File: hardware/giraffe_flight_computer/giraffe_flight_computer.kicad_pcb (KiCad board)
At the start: 4 copper layers, 170 parts, among them J1 BAT+, J10 HAT ADC CONNECT, J11 SHOE ADC, J12 BAT-, J2 BAT-, J3 PCM Interface, J4 EEPROM PROG, J5 PI_HEADER_HAT, J6 BAT+, J7 PI_HEADER_SHOE, J8 Extra Audio, J9 USB, Q1 DMG2305UX, Q2 DMMT5401, Q3 NPN, Q4 NPN, Q5 NPN, U1 DS18B20, U11 TPS61033, U12 ISO6720B, U13 PCM2902C, U14 INA180A1, U15 ISO6720B, U2 CAT24C32, U3 BMI088, U4 BME280, U5 TPS61033, U6 MAX11615, U7 INA180A1, U8 SAM-M8Q, U9 AD1582B, Y1 12MHz

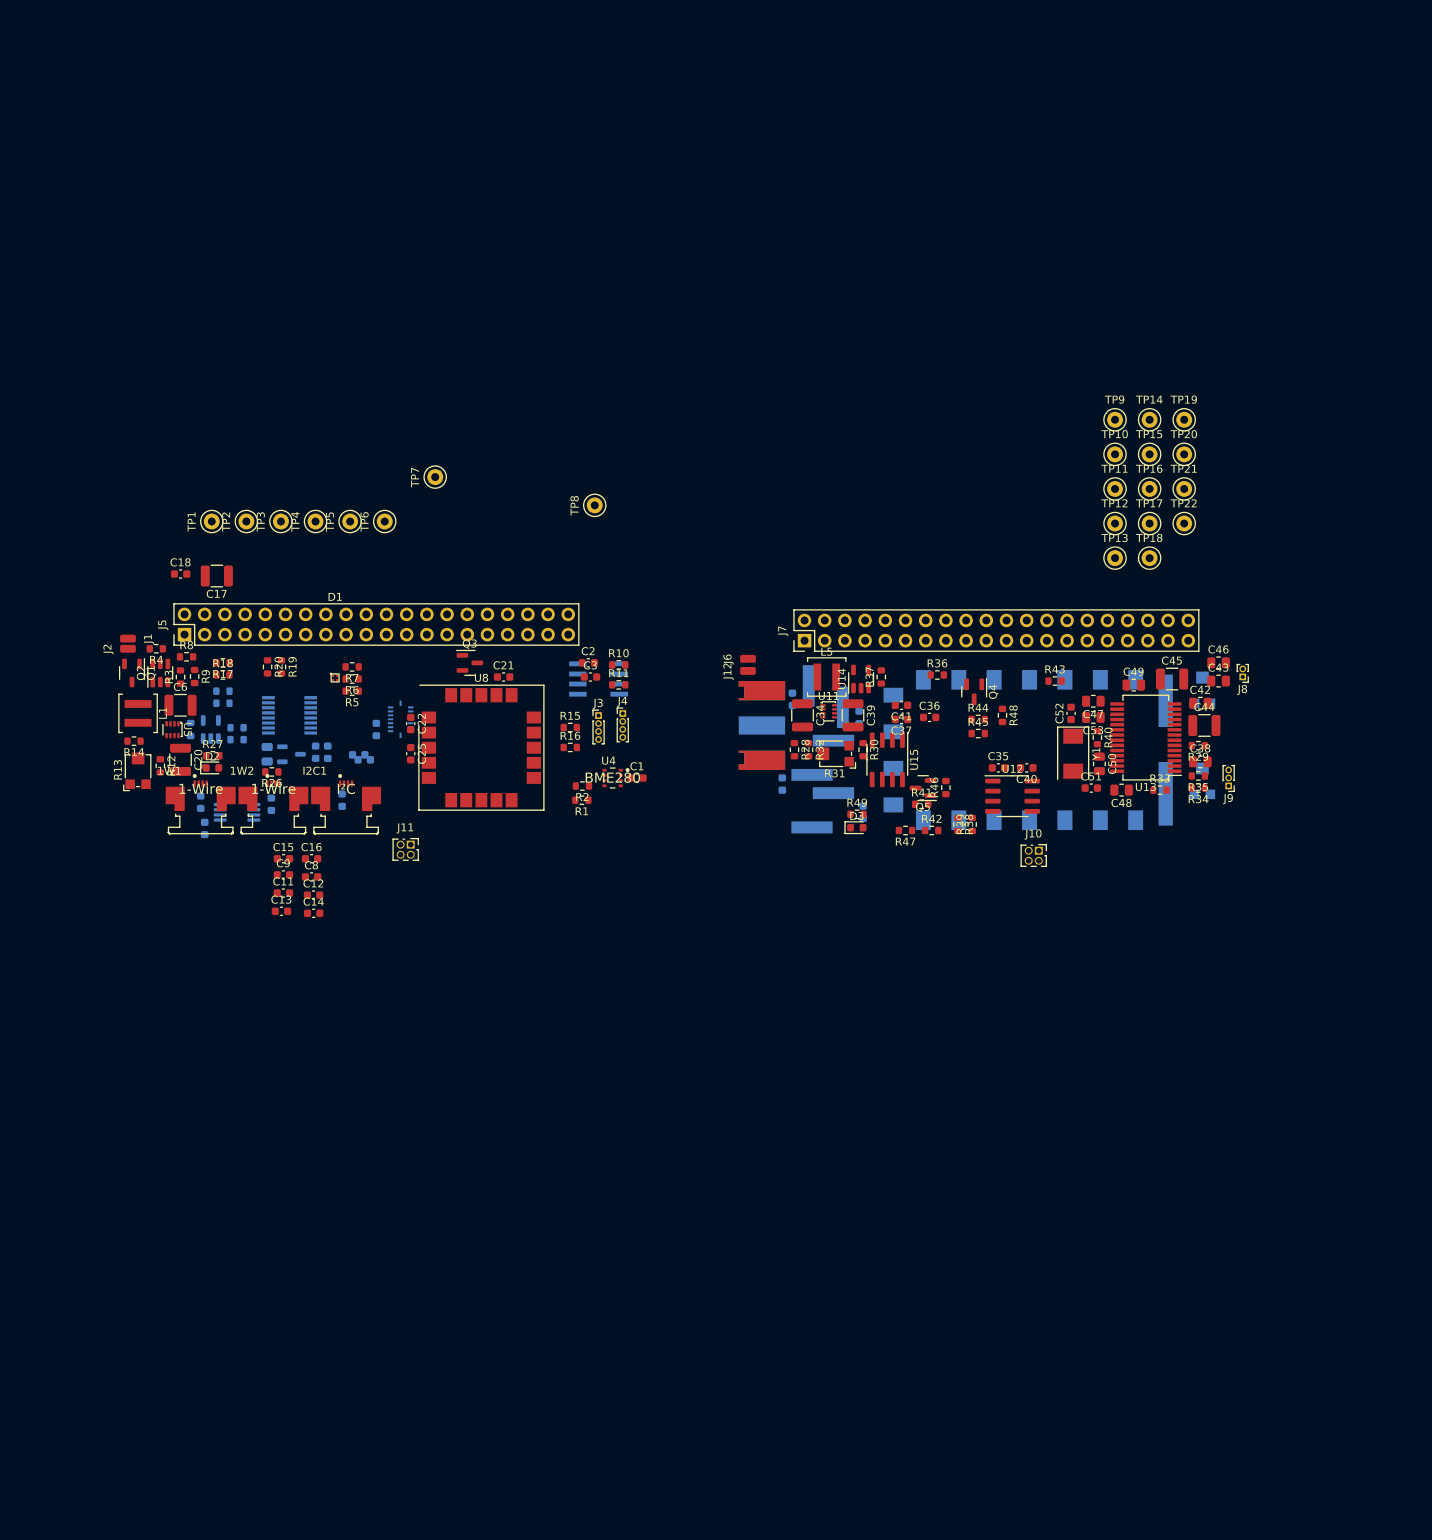
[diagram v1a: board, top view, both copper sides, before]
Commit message: More Schematic changes
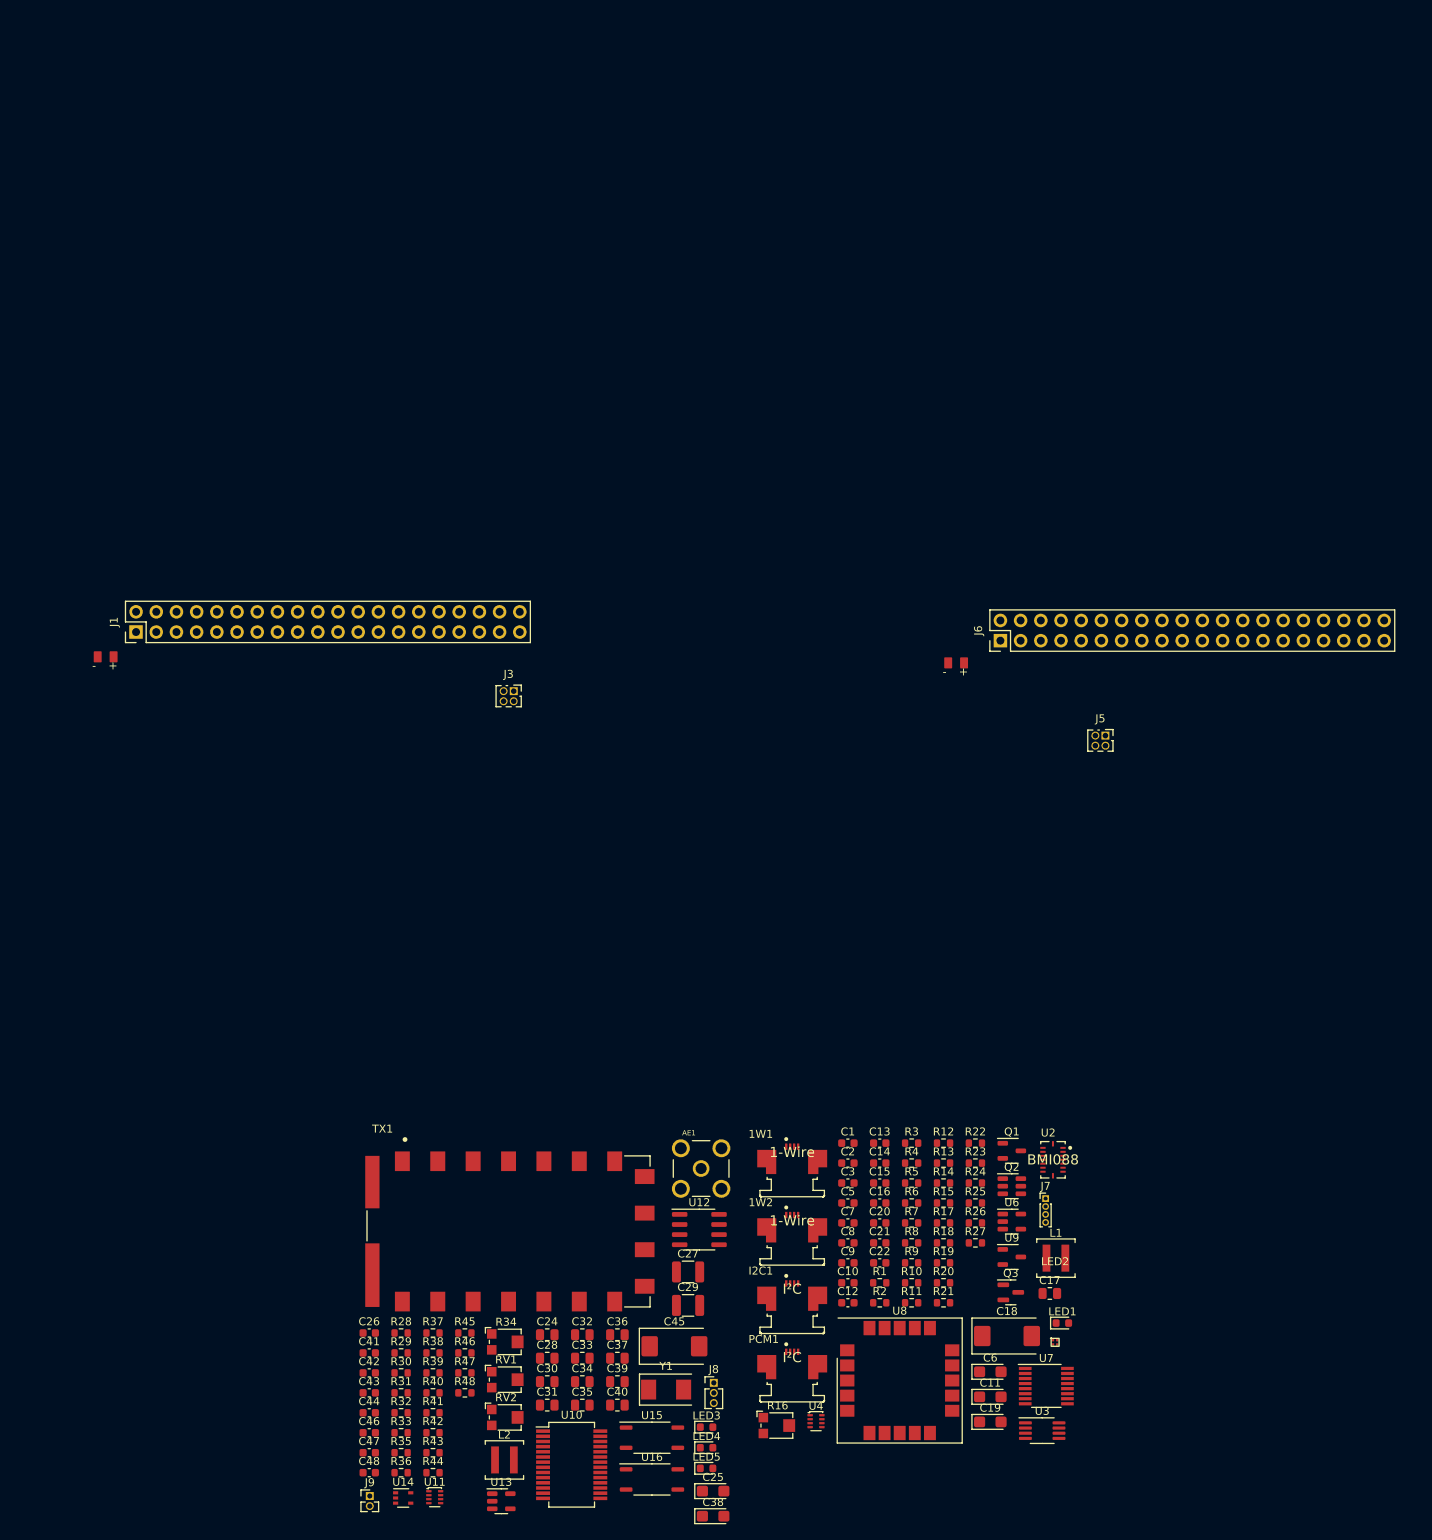
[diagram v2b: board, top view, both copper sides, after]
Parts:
- removed C23, C4: 0.1µF, Capacitor_SMD:C_0603_1608Metric
- removed C49, C50, C53: 1μF, Resistor_SMD:R_0805_2012Metric
- removed C51, C52: ?pF, Capacitor_SMD:C_0603_1608Metric
- removed D1: STATUS, giraffe_flight_computer_footprints:B36S3RGB LED
- removed D2: HAT PWR LED, LED_SMD:LED_0603_1608Metric
- removed D3: SHOE PWR LED, LED_SMD:LED_0603_1608Metric
- removed J10: HAT ADC CONNECT, Connector_PinSocket_1.27mm:PinSocket_2x02_P1.27mm_Vertical
- removed J11: SHOE ADC, Connector_PinSocket_1.27mm:PinSocket_2x02_P1.27mm_Vertical
- removed J12: BAT-, Connector_Wire:SolderWirePad_1x01_SMD_1x2mm
- removed L3: 68nH, giraffe_flight_computer_footprints:IND_AIAC-1812-33NK-T
- removed L4: 56nH, giraffe_flight_computer_footprints:IND_AIAC-1812-33NK-T
- removed L5: 0.47uH, Inductor_SMD:L_Coilcraft_XAL4020-XXX
- removed Q4, Q5: NPN, Package_TO_SOT_SMD:SOT-23
- removed R49: ?Ω, Resistor_SMD:R_0603_1608Metric
- removed TP1, TP10, TP11, TP12, TP13, TP14, TP15, TP16, TP17, TP18, TP19, TP2, TP20, TP21, TP22, TP3, TP4, TP5, TP6, TP7, TP8, TP9: ~, TestPoint:TestPoint_Keystone_5000-5004_Miniature
- removed U1: DS18B20, Package_SO:MSOP-8_3x3mm_P0.65mm
- removed U5: TPS61033, Package_TO_SOT_SMD:SOT-583-8
- added C10: 0.1µF, Capacitor_SMD:C_0603_1608Metric, F.Cu at (124.3, 104.9)
- added LED1: PWR, LED_SMD:LED_0603_1608Metric, F.Cu at (151.3, 110.0)
- added LED2: STATUS, giraffe_flight_computer_footprints:B36S3RGB LED, F.Cu at (150.4, 112.4)
- added LED3: PWR, LED_SMD:LED_0603_1608Metric, F.Cu at (106.6, 123.0)
- added LED4: RX, LED_SMD:LED_0603_1608Metric, F.Cu at (106.6, 125.6)
- added LED5: PTT, LED_SMD:LED_0603_1608Metric, F.Cu at (106.6, 128.2)
- added PCM1: I²C, giraffe_flight_computer_footprints:Molex-52745-0497, F.Cu at (117.3, 114.3)
- added U10: PCM2902C, Package_SO:SSOP-28_5.3x10.2mm_P0.65mm, F.Cu at (89.6, 127.8)
- added U16: TLP185, Package_SO:SOIC-4_4.55x3.7mm_P2.54mm, F.Cu at (99.7, 129.6)
- AE1: value SMA -> ~; footprint giraffe_flight_computer_footprints:MolexSmaConnector -> giraffe_flight_computer_footprints:LINX_CONSMA001-G; moved to F.Cu
- C11: value 100pF -> 10μF; footprint Capacitor_SMD:C_0603_1608Metric -> Capacitor_Tantalum_SMD:CP_EIA-3216-18_Kemet-A
- C12, C13, C14, C15, C16, C8, C9: value 100pF -> 0.1µF
- C17, C34: value 10μF -> 1μF; footprint Resistor_SMD:R_1210_3225Metric -> Resistor_SMD:R_0805_2012Metric
- C18: value 0.1µF -> 100μF; footprint Capacitor_SMD:C_0603_1608Metric -> Capacitor_Tantalum_SMD:CP_EIA-7343-31_Kemet-D
- C19: value 0.1µF -> 10μF; footprint Capacitor_SMD:C_0603_1608Metric -> Capacitor_Tantalum_SMD:CP_EIA-3216-18_Kemet-A; moved to F.Cu
- C20: value 10μF -> 0.1µF; footprint Resistor_SMD:R_1210_3225Metric -> Capacitor_SMD:C_0603_1608Metric
- C24, C5, C7, TX1, U9: moved to F.Cu
- C25: value 0.1µF -> 10μF; footprint Capacitor_SMD:C_0603_1608Metric -> Capacitor_Tantalum_SMD:CP_EIA-3216-18_Kemet-A
- C26: value 0.1µF -> 1μF; moved to F.Cu
- C27, C29: value 0.1µF -> 10μF; footprint Capacitor_SMD:C_0603_1608Metric -> Resistor_SMD:R_1210_3225Metric; moved to F.Cu
- C28: value 0.1µF -> 0.1μF; footprint Capacitor_SMD:C_0603_1608Metric -> Resistor_SMD:R_0805_2012Metric; moved to F.Cu
- C30: value 20pF -> 1uF; footprint Capacitor_SMD:C_0603_1608Metric -> Resistor_SMD:R_0805_2012Metric; moved to F.Cu
- C31: value 36pF -> 1μF; footprint Capacitor_SMD:C_0603_1608Metric -> Resistor_SMD:R_0805_2012Metric; moved to F.Cu
- C32: value 36pF -> 0.1μF; footprint Capacitor_SMD:C_0603_1608Metric -> Resistor_SMD:R_0805_2012Metric; moved to F.Cu
- C33: value 20pF -> 1μF; footprint Capacitor_SMD:C_0603_1608Metric -> Resistor_SMD:R_0805_2012Metric; moved to F.Cu
- C35, C36: value 0.1µF -> 1μF; footprint Capacitor_SMD:C_0603_1608Metric -> Resistor_SMD:R_0805_2012Metric
- C37: value 10kpF -> 1μF; footprint Capacitor_SMD:C_0603_1608Metric -> Resistor_SMD:R_0805_2012Metric
- C38: value 1μF -> 10μF; footprint Resistor_SMD:R_0805_2012Metric -> Capacitor_Tantalum_SMD:CP_EIA-3216-18_Kemet-A
- C39: value 10μF -> 0.1μF; footprint Resistor_SMD:R_1210_3225Metric -> Resistor_SMD:R_0805_2012Metric
- C40: value 0.1µF -> 0.1μF; footprint Capacitor_SMD:C_0603_1608Metric -> Resistor_SMD:R_0805_2012Metric
- C41: value 1kpF -> 0.1µF
- C42: value 1μF -> 10kpF; footprint Resistor_SMD:R_0805_2012Metric -> Capacitor_SMD:C_0603_1608Metric
- C43: value 1μF -> 1kpF; footprint Resistor_SMD:R_0805_2012Metric -> Capacitor_SMD:C_0603_1608Metric
- C44: value 10μF -> 20pF; footprint Resistor_SMD:R_1210_3225Metric -> Capacitor_SMD:C_0603_1608Metric
- C45: value 10μF -> 100μF; footprint Resistor_SMD:R_1210_3225Metric -> Capacitor_Tantalum_SMD:CP_EIA-7343-31_Kemet-D
- C46, C47: value 1μF -> 36pF; footprint Resistor_SMD:R_0805_2012Metric -> Capacitor_SMD:C_0603_1608Metric
- C48: value 1μF -> 20pF; footprint Resistor_SMD:R_0805_2012Metric -> Capacitor_SMD:C_0603_1608Metric
- C6: footprint Resistor_SMD:R_1210_3225Metric -> Capacitor_Tantalum_SMD:CP_EIA-3216-18_Kemet-A
- J1, J6: value BAT+ -> PI; footprint Connector_Wire:SolderWirePad_1x01_SMD_1x2mm -> giraffe_flight_computer_footprints:pi_zero
- J2: value BAT- -> BAT; footprint Connector_Wire:SolderWirePad_1x01_SMD_1x2mm -> giraffe_flight_computer_footprints:battery_connection
- J3: value PCM Interface -> ADC; footprint Connector_PinHeader_1.00mm:PinHeader_1x04_P1.00mm_Vertical -> Connector_PinSocket_1.27mm:PinSocket_2x02_P1.27mm_Vertical
- J4: value EEPROM PROG -> BAT; footprint Connector_PinHeader_1.00mm:PinHeader_1x04_P1.00mm_Vertical -> giraffe_flight_computer_footprints:battery_connection
- J5: value PI_HEADER_HAT -> ADC; footprint giraffe_flight_computer_footprints:pi_zero -> Connector_PinSocket_1.27mm:PinSocket_2x02_P1.27mm_Vertical
- J7: value PI_HEADER_SHOE -> ~; footprint giraffe_flight_computer_footprints:pi_zero -> Connector_PinHeader_1.00mm:PinHeader_1x04_P1.00mm_Vertical
- J8: value Extra Audio -> USB; footprint Connector_PinHeader_1.00mm:PinHeader_1x02_P1.00mm_Vertical -> Connector_PinHeader_1.27mm:PinHeader_1x03_P1.27mm_Vertical
- J9: value USB -> EXT_AUDIO; footprint Connector_PinHeader_1.00mm:PinHeader_1x03_P1.00mm_Vertical -> Connector_PinHeader_1.27mm:PinHeader_1x02_P1.27mm_Vertical
- L2: value 56nH -> 0.47uH; footprint giraffe_flight_computer_footprints:IND_AIAC-1812-33NK-T -> Inductor_SMD:L_Coilcraft_XAL4020-XXX; moved to F.Cu
- R1: value 0Ω -> ?Ω
- R10: value 3.9kΩ -> ?
- R11: value 3.9kΩ -> 4.7kΩ
- R12: value 21.5KΩ -> ?
- R13: value 1kΩ -> ?; footprint Potentiometer_SMD:Potentiometer_Bourns_TC33X_Vertical -> Resistor_SMD:R_0603_1608Metric
- R14: value 3kΩ -> 0Ω
- R15: value ?Ω -> 21.5k
- R16: value ?Ω -> 1k; footprint Resistor_SMD:R_0603_1608Metric -> Potentiometer_SMD:Potentiometer_Bourns_TC33X_Vertical
- R17: value ?Ω -> 3k
- R18, R48: value ?Ω -> 0Ω
- R19: value * -> ?Ω
- R2: value 0Ω -> ?
- R20: value * -> ?
- R21, R22, R23: value ?Ω -> ?; moved to F.Cu
- R24, R25: value ?Ω -> *; moved to F.Cu
- R26: value 4.7kΩ -> ?Ω
- R28: value ?Ω -> 22Ω
- R29: value 2.2Ω -> 22Ω
- R3, R37, R38, R41, R9: value ?Ω -> ?
- R30: value ?Ω -> 1.5kΩ
- R31: footprint Potentiometer_SMD:Potentiometer_Bourns_TC33X_Vertical -> Resistor_SMD:R_0603_1608Metric
- R32: value ?Ω -> 1MΩ
- R33: value 1.5kΩ -> ?k
- R34: value 22Ω -> ?k; footprint Resistor_SMD:R_0603_1608Metric -> Potentiometer_SMD:Potentiometer_Bourns_TC33X_Vertical
- R35: value 22Ω -> ?k
- R36: value 10kΩ -> ?Ω
- R39: value ?Ω -> 10kΩ
- R4, R5: value ?Ω -> 3.9kΩ
- R40: value 1MΩ -> ?
- R42: value ?Ω -> ?k
- R44, R47: value ?kΩ -> ?Ω
- RV1, RV2: value 100kΩ -> 100k; moved to F.Cu
- U13: value PCM2902C -> INA180A1; footprint Package_SO:SSOP-28_5.3x10.2mm_P0.65mm -> Package_TO_SOT_SMD:SOT-23-5
- U14: value INA180A1 -> 74LVC1G04; footprint Package_TO_SOT_SMD:SOT-23-5 -> Package_TO_SOT_SMD:SOT-353_SC-70-5
- U15: value ISO6720B -> TLP185; footprint Package_SO:SOIC-8_3.9x4.9mm_P1.27mm -> Package_SO:SOIC-4_4.55x3.7mm_P2.54mm
- U2: value CAT24C32 -> BMI088; footprint giraffe_flight_computer_footprints:CAT24C32WI_GT3 -> giraffe_flight_computer_footprints:BMI088; moved to F.Cu
- U3: value BMI088 -> DS18B20; footprint giraffe_flight_computer_footprints:BMI088 -> Package_SO:MSOP-8_3x3mm_P0.65mm; moved to F.Cu
- U4: value BME280 -> TPS61033; footprint giraffe_flight_computer_footprints:BME280 -> Package_TO_SOT_SMD:SOT-583-8
- U6: value MAX11615 -> INA180A1; footprint Package_SO:QSOP-16_3.9x4.9mm_P0.635mm -> Package_TO_SOT_SMD:SOT-23-5; moved to F.Cu
- U7: value INA180A1 -> MAX11615; footprint Package_TO_SOT_SMD:SOT-23-5 -> Package_SO:QSOP-16_3.9x4.9mm_P0.635mm; moved to F.Cu
- moved C46 144.2 mm to (64.1, 123.8)
- moved C18 141.4 mm to (144.3, 111.6)
- moved J9 140.2 mm to (64.2, 131.7), turned to 0 degrees
- moved C43 139.4 mm to (64.1, 118.7)
- moved C17 138.3 mm to (149.7, 106.2), turned to 0 degrees
- moved C44 136.0 mm to (64.1, 121.2)
- moved C42 134.2 mm to (64.1, 116.2)
- moved L1 134.2 mm to (150.5, 101.8), turned to 0 degrees
- moved U7 133.7 mm to (149.3, 117.9), turned to 0 degrees
- moved C6 131.9 mm to (142.2, 116.1)
- moved R35 131.5 mm to (68.1, 126.3), turned to 0 degrees
- moved C47 131.3 mm to (64.1, 126.3), turned to 0 degrees
- moved C48 127.8 mm to (64.1, 128.8), turned to 0 degrees
- moved R29 126.0 mm to (68.1, 113.7), turned to 0 degrees
- moved Q1 125.9 mm to (144.9, 88.3), turned to 0 degrees
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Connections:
- 1W1 pad 2: 1-Wire -> /hat/1_WIRE
- 1W1 pad 3: H_3V3 -> Net-(1W1-Pin_3)
- 1W2 pad 2: 1-Wire -> /hat/1_WIRE
- 1W2 pad 3: H_3V3 -> Net-(1W2-Pin_3)
- AE1 pad 1: /RF_OUT_FILTERED -> /shoe/RF_OUT_FILTERED
- C1 pad 1: H_GND -> H_3V3
- C1 pad 2: H_3V3 -> H_GND
- C11 pad 1: H_GND -> Net-(U4-VOUT)
- C11 pad 2: ADC CH2 -> H_GND
- C12 pad 1: H_GND -> H_3V3
- C12 pad 2: Net-(J11-Pin_2) -> Net-(1W2-Pin_3)
- C13 pad 1: H_GND -> H_3V3
- C13 pad 2: ADC CH1 -> H_GND
- C14 pad 1: H_GND -> H_3V3
- C14 pad 2: Net-(J11-Pin_3) -> H_GND
- C15 pad 1: H_GND -> H_3V3
- C15 pad 2: ADC CH0 -> H_GND
- C16 pad 1: H_GND -> H_3V3
- C16 pad 2: Net-(J11-Pin_4) -> H_GND
- C17 pad 1: H_5V_HAT -> Net-(U7-REF)
- C18 pad 1: H_GND -> H_5V_HAT
- C18 pad 2: H_5V_HAT -> H_GND
- C19 pad 1: H_3V3 -> H_5V_HAT
- C20 pad 1: Net-(U5-VOUT) -> H_GND
- C20 pad 2: H_GND -> H_5V_HAT
- C21 pad 1: H_3V3 -> H_5V_HAT
- C22 pad 1: H_3V3 -> H_5V_HAT
- C24 pad 1: Net-(U6-REF) -> S_5V
- C24 pad 2: H_GND -> S_GND
- C25 pad 1: H_3V3 -> /shoe/+BATT
- C25 pad 2: H_GND -> S_GND
- C26 pad 1: H_GND -> S_GND
- C26 pad 2: H_3V3 -> Net-(U10-SEL0)
- C27 pad 1: H_GND -> Net-(U10-VCCCI)
- C27 pad 2: H_3V3 -> S_GND
- C28 pad 1: H_5V_HAT -> S_GND
- C28 pad 2: H_GND -> S_3V3
- C29 pad 1: H_5V_HAT -> Net-(U10-VCOM)
- C29 pad 2: H_GND -> S_GND
- C30 pad 1: SA868_RF_OUT -> S_GND
- C30 pad 2: S_GND -> Net-(U10-VCCP1I)
- C31 pad 1: Net-(C31-Pad1) -> S_GND
- C31 pad 2: S_GND -> Net-(U10-VCCP2I)
- C32 pad 1: Net-(C32-Pad1) -> S_4V
- C33 pad 1: /RF_OUT_FILTERED -> S_GND
- C33 pad 2: S_GND -> Net-(U10-VCCXI)
- C34 pad 1: Net-(J6-Pin_1) -> Net-(U10-VOUTR)
- C34 pad 2: S_GND -> /shoe/AUDIO_IN_RIGHT
- C35 pad 1: S_3V3 -> Net-(U10-VINR)
- C35 pad 2: S_GND -> /shoe/AUDIO_OUT_RIGHT
- C36 pad 1: S_GND -> Net-(U10-VOUTL)
- C36 pad 2: S_4V -> /shoe/AUDIO_OUT_LEFT
- C37 pad 1: S_GND -> Net-(U10-VINL)
- C37 pad 2: S_4V -> /shoe/AUDIO_IN_LEFT
- C38 pad 1: /VBUS -> Net-(U11-VOUT)
- C39 pad 1: Net-(U11-VOUT) -> Net-(U10-XTI)
- C40 pad 1: S_4V -> Net-(U10-XTO)
- C42 pad 1: Net-(U13-VINL) -> S_GND
- C42 pad 2: PCM_AUDIO.IN_L -> S_4V
- C43 pad 1: Net-(U13-VINR) -> S_GND
- C43 pad 2: PCM_AUDIO.IN_R -> S_4V
- C44 pad 1: Net-(U13-VCCCI) -> Net-(TX1-ANT)
- C45 pad 1: Net-(U13-VCOM) -> S_4V
- C46 pad 1: Net-(U13-VOUTR) -> Net-(C46-Pad1)
- C46 pad 2: PCM_AUDIO.OUT_R -> S_GND
- C47 pad 1: Net-(U13-VCCP1I) -> Net-(C47-Pad1)
- C48 pad 1: Net-(U13-SEL0) -> /shoe/RF_OUT_FILTERED
- C6 pad 1: /Battery Polarized -> Net-(Q1-S)
- C8 pad 2: ADC CH3 -> H_3V3
- C9 pad 2: Net-(J11-Pin_1) -> H_3V3
- I2C1 pad 3: I2C0.SCL -> /hat/I2C0.SCL
- I2C1 pad 4: I2C0.SDA -> /hat/I2C0.SDA
- J1 pad 1: Net-(J1-Pin_1) -> /hat/3V3
- J2 pad 1: H_GND -> /hat/-BATT
- J3 pad 1: /PCM.DOUT -> /hat/ADC.CH4
- J3 pad 2: /PCM.DIN -> /hat/ADC.CH5
- J3 pad 3: /PCM.FS -> /hat/ADC.CH6
- J3 pad 4: /PCM.CLK -> /hat/ADC.CH7
- J4 pad 1: H_GND -> /shoe/-BATT
- J4 pad 2: H_3V3 -> /shoe/+BATT
- J5 pad 1: H_3V3 -> /shoe/ADC_CH4
- J5 pad 2: H_5V_HAT -> /shoe/ADC_CH5
- J5 pad 3: I2C0.SDA -> unconnected-(J5-Pin_3-Pad3)
- J5 pad 4: H_5V_HAT -> unconnected-(J5-Pin_4-Pad4)
- J6 pad 1: Net-(J6-Pin_1) -> /shoe/3V3
- J7 pad 1: S_3V3 -> H_GND
- J7 pad 2: S_5V -> H_3V3
- J7 pad 3: unconnected-(J7-SDA/GPIO2-Pad3) -> /hat/EEPROM.SCL
- J7 pad 4: S_5V -> /hat/EEPROM.SDA
- J8 pad 1: PCM_AUDIO.IN_R -> S_GND
- J8 pad 2: PCM_AUDIO.OUT_R -> Net-(J8-Pin_2)
- J9 pad 1: Net-(J9-Pin_1) -> S_GND
- J9 pad 2: Net-(J9-Pin_2) -> /shoe/AUDIO_OUT_RIGHT
- L1 pad 1: /Battery Polarized -> Net-(Q1-S)
- L1 pad 2: Net-(U5-SW) -> Net-(U4-SW)
- L2 pad 1: SA868_RF_OUT -> /shoe/+BATT
- L2 pad 2: Net-(C31-Pad1) -> Net-(U11-SW)
- Q1 pad 1: Net-(J1-Pin_1) -> /hat/+BATT
- Q1 pad 3: /Battery Polarized -> Net-(Q1-S)
- Q2 pad 5: /Battery Polarized -> Net-(Q1-S)
- Q2 pad 6: Net-(J1-Pin_1) -> /hat/+BATT
- R1 pad 1: H_3V3 -> H_5V_HAT
- R1 pad 2: Net-(U4-SDO) -> Net-(LED1-A)
- R10 pad 1: EEPROM.SDA -> Net-(U7-AIN0)
- R10 pad 2: H_3V3 -> H_GND
- R11 pad 1: EEPROM.SCL -> H_3V3
- R11 pad 2: H_3V3 -> /hat/1_WIRE
- R12 pad 1: Net-(U5-VOUT) -> /hat/3V3
- R12 pad 2: Net-(R12-Pad2) -> Net-(U7-AIN3)
- R13 pad 1: Net-(R12-Pad2) -> Net-(U7-AIN3)
- R13 pad 2: Net-(U5-FB) -> H_GND
- R14 pad 1: Net-(U5-FB) -> Net-(U5-SDO)
- R15 pad 1: Net-(Q3-C) -> Net-(U4-VOUT)
- R15 pad 2: H_3V3 -> Net-(R15-Pad2)
- R16 pad 1: Net-(Q3-B) -> Net-(R15-Pad2)
- R16 pad 2: SAM-M8Q.RST -> Net-(U4-FB)
- R17 pad 1: H_3V3 -> Net-(U4-FB)
- R17 pad 2: ADC CH3 -> H_GND
- R18 pad 1: ADC CH3 -> Net-(U5-SDO)
- R18 pad 2: H_GND -> H_3V3
- R19 pad 1: I2C0.SDA -> Net-(U4-VOUT)
- R19 pad 2: H_3V3 -> H_5V_HAT
- R2 pad 1: Net-(U4-SDO) -> Net-(Q2-B1)
- R20 pad 1: H_3V3 -> Net-(U6-OUT)
- R20 pad 2: I2C0.SCL -> Net-(U7-AIN1)
- R21 pad 1: Net-(U5-VOUT) -> Net-(U7-AIN1)
- R21 pad 2: H_5V_HAT -> H_GND
- R22 pad 1: Net-(U7-OUT) -> H_5V_HAT
- R22 pad 2: ADC CH1 -> Net-(U7-AIN2)
- R23 pad 1: ADC CH1 -> Net-(U7-AIN2)
- R24 pad 1: H_5V_HAT -> /hat/I2C0.SDA
- R24 pad 2: ADC CH2 -> H_3V3
- R25 pad 1: ADC CH2 -> H_3V3
- R25 pad 2: H_GND -> /hat/I2C0.SCL
- R26 pad 1: H_3V3 -> Net-(Q3-C)
- R26 pad 2: 1-Wire -> H_3V3
- R27 pad 1: H_5V_HAT -> Net-(Q3-B)
- R27 pad 2: Net-(D2-A) -> /hat/SAM_M8Q.RST
- R28 pad 1: SA868.PWR -> Net-(J8-Pin_3)
- R28 pad 2: S_GND -> Net-(U10-D+)
- R29 pad 1: S_5V -> Net-(J8-Pin_2)
- R29 pad 2: /VBUS -> Net-(U10-D-)
- R3 pad 1: Net-(Q2-B1) -> Net-(Q1-G)
- R30 pad 1: Net-(U11-VOUT) -> Net-(U10-SEL0)
- R30 pad 2: Net-(R30-Pad2) -> Net-(U10-D+)
- R31 pad 1: Net-(R30-Pad2) -> /shoe/SA868_PWR_CTRL
- R31 pad 2: Net-(U11-FB) -> S_GND
- R32 pad 1: Net-(U11-FB) -> Net-(U10-XTO)
- R32 pad 2: S_GND -> Net-(U10-XTI)
- R33 pad 1: Net-(U13-SEL0) -> Net-(U11-VOUT)
- R33 pad 2: Net-(J9-Pin_1) -> Net-(R33-Pad2)
- R34 pad 1: Net-(J9-Pin_1) -> Net-(R33-Pad2)
- R34 pad 2: Net-(U13-D+) -> Net-(U11-FB)
- R35 pad 1: Net-(J9-Pin_2) -> Net-(U11-FB)
- R35 pad 2: Net-(U13-D-) -> S_GND
- R36 pad 1: S_4V -> Net-(U11-VOUT)
- R36 pad 2: Net-(TX1-PD) -> S_4V
- R37 pad 1: Net-(U11-VOUT) -> Net-(U13-OUT)
- R37 pad 2: S_4V -> /shoe/ADC_CH4
- R38 pad 1: Net-(U14-OUT) -> /shoe/ADC_CH4
- R38 pad 2: ADC CH4 -> S_GND
- R39 pad 1: ADC CH4 -> Net-(TX1-PD)
- R39 pad 2: S_GND -> S_4V
- R4 pad 1: Net-(Q1-G) -> /hat/EEPROM.SDA
- R4 pad 2: H_GND -> H_3V3
- R40 pad 1: Net-(U13-XTO) -> S_4V
- R40 pad 2: Net-(U13-XTI) -> /shoe/ADC_CH5
- R41 pad 1: S_4V -> /shoe/ADC_CH5
- R41 pad 2: ADC CH5 -> S_GND
- R42 pad 1: ADC CH5 -> Net-(TX1-PTT)
- R42 pad 2: S_GND -> Net-(R42-Pad2)
- R43 pad 1: Net-(Q5-B) -> Net-(R43-Pad1)
- R44 pad 1: S_GND -> S_4V
- R44 pad 2: Net-(Q4-B) -> Net-(LED3-A)
- R45 pad 1: Net-(Q4-C) -> /shoe/SA868_RX
- R45 pad 2: S_4V -> Net-(LED4-A)
- R46 pad 1: S_4V -> /shoe/SA868_PTT
- R46 pad 2: Net-(Q5-C) -> Net-(R46-Pad2)
- R47 pad 1: S_GND -> /shoe/SA868_PTT
- R47 pad 2: Net-(Q5-B) -> Net-(LED5-A)
- R48 pad 1: Net-(Q4-B) -> S_GND
- R48 pad 2: Net-(U15-OUTB) -> Net-(TX1-H/L)
- R5 pad 1: /Status LED Red -> /hat/EEPROM.SCL
- R5 pad 2: Net-(D1-RK) -> H_3V3
- R6 pad 1: /Status LED Green -> /hat/STATUS_LED.RED
- R7 pad 1: /Status LED Blue -> /hat/STATUS_LED.GREEN
- R8 pad 1: /Battery Polarized -> /hat/STATUS_LED.BLUE
- R8 pad 2: ADC CH0 -> Net-(LED2-BA)
- R9 pad 1: ADC CH0 -> Net-(Q1-S)
- R9 pad 2: H_GND -> Net-(U7-AIN0)
- RV1 pad 2: SA868_AUDIO_OUT -> Net-(TX1-MIC_IN)
- RV1 pad 3: PCM_AUDIO.IN_L -> /shoe/AUDIO_OUT_LEFT
- RV2 pad 2: PCM_AUDIO.OUT_L -> /shoe/AUDIO_IN_LEFT
- RV2 pad 3: SA868_AUDIO_IN -> Net-(TX1-AF_OUT)
- TX1 pad 12: SA868_RF_OUT -> Net-(TX1-ANT)
- TX1 pad 18: SA868_AUDIO_IN -> Net-(TX1-MIC_IN)
- TX1 pad 3: SA868_AUDIO_OUT -> Net-(TX1-AF_OUT)
- TX1 pad 5: Net-(Q4-C) -> Net-(TX1-PTT)
- TX1 pad 7: Net-(SW2-B) -> Net-(TX1-H/L)
- U11 pad 1: Net-(J6-Pin_1) -> /shoe/+BATT
- U11 pad 2: SA868.PWR -> /shoe/SA868_PWR_CTRL
- U12 pad 2: UART.RXD -> /shoe/UART.RX
- U12 pad 3: UART.TXD -> /shoe/UART.TX
- U13 pad 1: Net-(U13-D+) -> Net-(U13-OUT)
- U13 pad 2: Net-(U13-D-) -> S_GND
- U13 pad 3: /VBUS -> Net-(U11-VOUT)
- U13 pad 4: S_GND -> S_4V
- U13 pad 5: unconnected-(U13-HID0-Pad5) -> S_5V
- U14 pad 1: Net-(U14-OUT) -> (no net)
- U14 pad 2: S_GND -> Net-(U14-Pad2)
- U14 pad 3: Net-(U11-VOUT) -> S_GND
- U14 pad 4: S_4V -> Net-(R42-Pad2)
- U14 pad 5: S_5V -> S_4V
- U15 pad 1: S_3V3 -> Net-(R43-Pad1)
- U15 pad 3: SA868.PTT -> S_GND
- U15 pad 4: S_GND -> /shoe/SA868_RX
- U15 pad 6: Net-(U15-OUTB) -> S_3V3
- U2 pad 1: H_GND -> unconnected-(U2-INT2-Pad1)
- U2 pad 3: H_GND -> H_3V3
- U2 pad 5: EEPROM.SDA -> /hat/SPI0.CE1
- U2 pad 6: EEPROM.SCL -> H_GND
- U2 pad 7: unconnected-(U2-WP-Pad7) -> H_GND
- U2 pad 8: H_3V3 -> /hat/SPI0.SCLK
- U3 pad 2: H_GND -> unconnected-(U3-NC-Pad2)
- U3 pad 4: H_GND -> /hat/1_WIRE
- U3 pad 5: SPI0.CE1 -> H_GND
- U3 pad 6: H_GND -> unconnected-(U3-NC-Pad6)
- U3 pad 7: H_GND -> unconnected-(U3-NC-Pad7)
- U3 pad 8: SPI0.SCLK -> unconnected-(U3-NC-Pad8)
- U4 pad 1: H_GND -> Net-(Q1-S)
- U4 pad 2: H_3V3 -> Net-(Q1-S)
- U4 pad 3: I2C0.SDA -> H_GND
- U4 pad 4: I2C0.SCL -> Net-(U4-PG)
- U4 pad 5: Net-(U4-SDO) -> Net-(U4-FB)
- U4 pad 6: H_3V3 -> H_GND
- U4 pad 7: H_GND -> Net-(U4-SW)
- U4 pad 8: H_3V3 -> Net-(U4-VOUT)
- U6 pad 1: Net-(U6-REF) -> Net-(U6-OUT)
- U6 pad 2: unconnected-(U6-NC-Pad2) -> H_GND
- U6 pad 3: unconnected-(U6-NC-Pad3) -> Net-(U4-VOUT)
- U6 pad 4: unconnected-(U6-NC-Pad4) -> H_5V_HAT
- U6 pad 5: ADC CH0 -> H_5V_HAT
- U7 pad 1: Net-(U7-OUT) -> Net-(U7-REF)
- U7 pad 2: H_GND -> unconnected-(U7-NC-Pad2)
- U7 pad 3: Net-(U5-VOUT) -> unconnected-(U7-NC-Pad3)
- U7 pad 4: H_5V_HAT -> unconnected-(U7-NC-Pad4)
- U7 pad 5: H_5V_HAT -> Net-(U7-AIN0)
- U8 pad 12: I2C0.SCL -> /hat/I2C0.SCL
- U8 pad 13: SAM-M8Q.TX_RDY -> /hat/SAM_M8Q.TX_RDY
- U8 pad 9: I2C0.SDA -> /hat/I2C0.SDA
- U9 pad 1: Net-(U6-REF) -> Net-(U7-REF)
- Y1 pad 1: Net-(U13-XTO) -> Net-(U10-XTO)
- Y1 pad 2: Net-(U13-XTI) -> Net-(U10-XTI)

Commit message: Rev A Hat Complete
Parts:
- removed C12: 0.1µF, Capacitor_SMD:C_0603_1608Metric
- removed Q1: DMG2305UX, Package_TO_SOT_SMD:SOT-23-3
- removed Q2: DMMT5401, Package_TO_SOT_SMD:SOT-23-6
- removed R21, R37, R38: ?, Resistor_SMD:R_0603_1608Metric
- removed R31, R36: ?Ω, Resistor_SMD:R_0603_1608Metric
- removed R34: ?k, Potentiometer_SMD:Potentiometer_Bourns_TC33X_Vertical
- removed U13, U6: INA180A1, Package_TO_SOT_SMD:SOT-23-5
- added C4: 0.1µF, Capacitor_SMD:C_0603_1608Metric, B.Cu at (44.7, 40.5)
- added J10: BATT_C, Connector_PinHeader_1.00mm:PinHeader_1x03_P1.00mm_Vertical, F.Cu at (27.8, 40.0)
- added L3: 56uH, giraffe_flight_computer_footprints:Murata-LQH3NPH_ME-0-0-MFG, B.Cu at (132.8, 41.5)
- added L4: 68uH, giraffe_flight_computer_footprints:Murata-LQH3NPH_ME-0-0-MFG, B.Cu at (129.5, 36.5)
- added L5: 56uH, giraffe_flight_computer_footprints:Murata-LQH3NPH_ME-0-0-MFG, B.Cu at (125.8, 36.5)
- added TP2: GND, TestPoint:TestPoint_Keystone_5015_Micro-Minature, F.Cu at (126.5, 46.2)
- added TP3: GND, TestPoint:TestPoint_Keystone_5015_Micro-Minature, F.Cu at (54.4, 43.6)
- added TP9: ~, TestPoint:TestPoint_Pad_1.0x1.0mm, F.Cu at (136.8, 46.8)
- added U1: CAT24C32, giraffe_flight_computer_footprints:CAT24C32WI_GT3, B.Cu at (87.9, 24.1)
- added U5: BME280, giraffe_flight_computer_footprints:BME280, F.Cu at (88.2, 39.5)
- 1W1: value 1-Wire -> 1W1; moved to B.Cu
- 1W2: value 1-Wire -> 1W2; moved to B.Cu
- AE1: footprint giraffe_flight_computer_footprints:LINX_CONSMA001-G -> giraffe_flight_computer_footprints:MolexSmaConnector; moved to B.Cu
- C1, C10, C16, C18, C2, C3, C36, C37, C41, C42, C43, C44, C46, C47, C48, C9, I2C1, Q3, R12, R13, R24, R25, R26, R27, R3, RV1, RV2, TX1, U2, U7: moved to B.Cu
- J5: footprint Connector_PinSocket_1.27mm:PinSocket_2x02_P1.27mm_Vertical -> Connector_PinHeader_1.27mm:PinHeader_1x01_P1.27mm_Vertical
- J8: footprint Connector_PinHeader_1.27mm:PinHeader_1x03_P1.27mm_Vertical -> Connector_PinHeader_1.00mm:PinHeader_1x03_P1.00mm_Vertical
- J9: footprint Connector_PinHeader_1.27mm:PinHeader_1x02_P1.27mm_Vertical -> Connector_PinHeader_1.00mm:PinHeader_1x03_P1.00mm_Vertical
- PCM1: value I²C -> PCM; footprint giraffe_flight_computer_footprints:Molex-52745-0497 -> Connector_PinHeader_1.27mm:PinHeader_1x04_P1.27mm_Vertical
- R19: value ?Ω -> ?k; footprint Resistor_SMD:R_0603_1608Metric -> Potentiometer_SMD:Potentiometer_Bourns_TC33X_Vertical
- R20: value ? -> ?Ω
- moved J9 160.0 mm to (179.5, 20.8), turned to -90 degrees
- moved C19 150.6 mm to (30.0, 22.0), turned to -90 degrees
- moved C18 144.0 mm to (30.5, 23.4), turned to 90 degrees
- moved L1 139.9 mm to (31.0, 29.0)
- moved C6 139.6 mm to (29.5, 33.8), turned to -90 degrees
- moved U7 138.8 mm to (38.8, 34.0), turned to 90 degrees
- moved C11 137.5 mm to (34.8, 33.5), turned to -90 degrees
- moved U3 134.0 mm to (40.5, 44.5), turned to -90 degrees
- moved U14 133.4 mm to (150.8, 27.0), turned to 180 degrees
- moved R29 131.8 mm to (177.3, 39.9), turned to 180 degrees
- moved C35 130.5 mm to (178.8, 23.8), turned to 90 degrees
- moved LED2 130.0 mm to (50.2, 29.5), turned to 180 degrees
- moved RV1 129.9 mm to (178.0, 30.2), turned to -90 degrees
- moved R43 129.9 mm to (159.3, 30.0), turned to 90 degrees
- moved R28 129.6 mm to (177.3, 41.4), turned to 180 degrees
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- renumbered LED1 to PWR
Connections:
- net /shoe/RF_OUT_FILTERED renamed Net-(AE1-A)
- net Net-(U4-SW) renamed /hat/BOOST_SW
- net Net-(U7-AIN0) renamed /hat/ADC.CH0
- net Net-(U7-AIN2) renamed /hat/ADC.CH2
- net Net-(U7-AIN3) renamed /hat/ADC.CH3
- 1W1 pad 3: Net-(1W1-Pin_3) -> H_3V3
- 1W1 pad 4: (no net) -> unconnected-(1W1-Pin_4-Pad4)
- 1W1 pad MP1: (no net) -> unconnected-(1W1-Mount_Point-PadMP1)
- 1W1 pad MP2: (no net) -> unconnected-(1W1-Mount_Point-PadMP2)
- 1W2 pad 3: Net-(1W2-Pin_3) -> H_3V3
- 1W2 pad 4: (no net) -> unconnected-(1W2-Pin_4-Pad4)
- 1W2 pad MP1: (no net) -> unconnected-(1W2-Mount_Point-PadMP1)
- 1W2 pad MP2: (no net) -> unconnected-(1W2-Mount_Point-PadMP2)
- C10 pad 1: H_3V3 -> H_GND
- C10 pad 2: Net-(1W1-Pin_3) -> H_3V3
- C11 pad 1: Net-(U4-VOUT) -> H_5V
- C18 pad 1: H_5V_HAT -> H_5V
- C19 pad 1: H_5V_HAT -> H_5V
- C20 pad 2: H_5V_HAT -> H_5V
- C21 pad 1: H_5V_HAT -> H_5V
- C22 pad 1: H_5V_HAT -> H_5V
- C38 pad 1: Net-(U11-VOUT) -> S_4V
- C6 pad 1: Net-(Q1-S) -> /hat/+BATT
- I2C1 pad MP1: (no net) -> unconnected-(I2C1-Mount_Point-PadMP1)
- I2C1 pad MP2: (no net) -> unconnected-(I2C1-Mount_Point-PadMP2)
- J1 pad 1: /hat/3V3 -> H_3V3
- J1 pad 11: /hat/STATUS_LED.RED -> /hat/STATUS_LED.BLUE
- J1 pad 14: /hat/-BATT -> H_GND
- J1 pad 15: /hat/STATUS_LED.BLUE -> /hat/STATUS_LED.RED
- J1 pad 17: /hat/3V3 -> H_3V3
- J1 pad 2: /hat/5V -> H_5V
- J1 pad 20: /hat/-BATT -> H_GND
- J1 pad 25: /hat/-BATT -> H_GND
- J1 pad 29: /hat/BMI088.INT1 -> /hat/BMI088.INT3
- J1 pad 30: /hat/-BATT -> H_GND
- J1 pad 31: /hat/BMI088.INT3 -> /hat/BMI088.INT1
- J1 pad 32: /hat/SAM_M8Q.TX_RDY -> /hat/SAM_M8Q.RST
- J1 pad 33: /hat/SAM_M8Q.RST -> /hat/SAM_M8Q.TX_RDY
- J1 pad 34: /hat/-BATT -> H_GND
- J1 pad 39: /hat/-BATT -> H_GND
- J1 pad 4: /hat/5V -> H_5V
- J1 pad 6: /hat/-BATT -> H_GND
- J1 pad 9: /hat/-BATT -> H_GND
- J2 pad 1: /hat/-BATT -> H_GND
- J4 pad 1: /shoe/-BATT -> S_GND
- J6 pad 1: /shoe/3V3 -> S_3V3
- J6 pad 14: /shoe/-BATT -> S_GND
- J6 pad 17: /shoe/3V3 -> S_3V3
- J6 pad 2: /shoe/5V -> S_5V
- J6 pad 20: /shoe/-BATT -> S_GND
- J6 pad 25: /shoe/-BATT -> S_GND
- J6 pad 30: /shoe/-BATT -> S_GND
- J6 pad 34: /shoe/-BATT -> S_GND
- J6 pad 39: /shoe/-BATT -> S_GND
- J6 pad 4: /shoe/5V -> S_5V
- J6 pad 6: /shoe/-BATT -> S_GND
- J6 pad 9: /shoe/-BATT -> S_GND
- L1 pad 1: Net-(Q1-S) -> /hat/+BATT
- LED3 pad 1: H_GND -> S_GND
- LED4 pad 1: H_GND -> S_GND
- LED5 pad 1: H_GND -> S_GND
- R1 pad 1: H_5V_HAT -> H_5V
- R12 pad 1: /hat/3V3 -> H_3V3
- R15 pad 1: Net-(U4-VOUT) -> H_5V
- R16 pad 1: Net-(R15-Pad2) -> Net-(U4-FB)
- R16 pad 2: Net-(U4-FB) -> Net-(R15-Pad2)
- R16 pad 3: (no net) -> unconnected-(R16-Pad3)
- R19 pad 1: Net-(U4-VOUT) -> Net-(U11-FB)
- R19 pad 2: H_5V_HAT -> Net-(R19-Pad2)
- R2 pad 2: H_GND -> /hat/ADC.CH1
- R20 pad 1: Net-(U6-OUT) -> Net-(U11-EN)
- R20 pad 2: Net-(U7-AIN1) -> /shoe/SA868_PWR_CTRL
- R22 pad 1: H_5V_HAT -> H_5V
- R3 pad 1: Net-(Q1-G) -> /hat/ADC.CH1
- R33 pad 1: Net-(U11-VOUT) -> S_4V
- R33 pad 2: Net-(R33-Pad2) -> Net-(R19-Pad2)
- R40 pad 2: /shoe/ADC_CH5 -> /shoe/ADC_CH4
- R41 pad 1: /shoe/ADC_CH5 -> /shoe/ADC_CH4
- R9 pad 1: Net-(Q1-S) -> /hat/+BATT
- TX1 pad 11: (no net) -> unconnected-(TX1-NC-Pad11)
- TX1 pad 13: (no net) -> unconnected-(TX1-NC-Pad13)
- TX1 pad 14: (no net) -> unconnected-(TX1-NC-Pad14)
- TX1 pad 15: (no net) -> unconnected-(TX1-NC-Pad15)
- TX1 pad 2: (no net) -> unconnected-(TX1-NC-Pad2)
- TX1 pad 4: (no net) -> unconnected-(TX1-NC-Pad4)
- TX1 pad P2: (no net) -> unconnected-(TX1-NC-PadP2)
- TX1 pad P3: (no net) -> unconnected-(TX1-NC-PadP3)
- U11 pad 2: /shoe/SA868_PWR_CTRL -> Net-(U11-EN)
- U11 pad 4: Net-(U11-PG) -> unconnected-(U11-PG-Pad4)
- U11 pad 8: Net-(U11-VOUT) -> S_4V
- U14 pad 1: (no net) -> unconnected-(U14-NC-Pad1)
- U16 pad 3: H_GND -> S_GND
- U4 pad 1: Net-(Q1-S) -> /hat/+BATT
- U4 pad 2: Net-(Q1-S) -> /hat/+BATT
- U4 pad 4: Net-(U4-PG) -> unconnected-(U4-PG-Pad4)
- U4 pad 8: Net-(U4-VOUT) -> H_5V
- U7 pad 6: Net-(U7-AIN1) -> /hat/ADC.CH1
- U9 pad 3: H_5V_HAT -> H_5V
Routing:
- net /hat/I2C0.SCL: track 0.00 -> 86.5 mm, vias 0 -> 5
- net /hat/I2C0.SDA: track 0.00 -> 85.2 mm, vias 0 -> 4
- net H_5V: track 0.00 -> 83.9 mm, vias 0 -> 4
- net S_5V: track 0.00 -> 81.8 mm
- net S_4V: track 0.00 -> 71.0 mm, vias 0 -> 9
- net H_3V3: track 0.00 -> 61.5 mm, vias 0 -> 19
- net S_3V3: track 0.00 -> 53.2 mm, vias 0 -> 2
- net /hat/ADC.CH5: track 0.00 -> 41.7 mm, vias 0 -> 2
- net /shoe/UART.TX: track 0.00 -> 41.5 mm, vias 0 -> 1
- net /hat/ADC.CH4: track 0.00 -> 40.8 mm, vias 0 -> 1
- net /hat/ADC.CH7: track 0.00 -> 40.7 mm, vias 0 -> 1
- net /hat/ADC.CH6: track 0.00 -> 39.3 mm, vias 0 -> 1
- net /hat/EEPROM.SDA: track 0.00 -> 38.8 mm, vias 0 -> 1
- net /hat/PCM.CLK: track 0.00 -> 38.5 mm
- net /shoe/UART.RX: track 0.00 -> 37.2 mm, vias 0 -> 1
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- added copper zone on F.Cu, net /hat/+BATT
- added copper zone on F.Cu, net /hat/BOOST_SW
- added copper zone on F.Cu, net /shoe/+BATT
- added copper zone on In1.Cu, net H_3V3
- added copper zone on F.Cu, net H_5V
- added copper zone on B.Cu, net H_GND
- added copper zone on F.Cu, net H_GND
- added copper zone on In2.Cu, net H_GND
- added copper zone on F.Cu, net Net-(U11-SW)
- added copper zone on B.Cu, net S_4V
- added copper zone on F.Cu, net S_4V
- added copper zone on B.Cu, net S_GND
- added copper zone on F.Cu, net S_GND
- added copper zone on In1.Cu, net S_GND
- added copper zone on In2.Cu, net S_GND
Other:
- board outline added: 65 x 30 mm
- board text added: "0x76"
- board text added: "0x77"
- board text added: "1-W EXT0"
- board text added: "1-W EXT1"
- board text added: "3v3"
- board text added: "5V ADC GND"
- board text added: "ADC"
- board text added: "BMI088"
- board text added: "CH6 CH4"
- board text added: "CH7 CH5"
- board text added: "CK"
- board text added: "EEPROM PROG"
- board text added: "EXT ADC"
- board text added: "FS"
- board text added: "GND"
- board text added: "I2C EXT"
- board text added: "IN"
- board text added: "OT"
- board text added: "SCL"
- board text added: "SDA"
